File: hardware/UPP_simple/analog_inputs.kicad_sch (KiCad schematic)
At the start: 103 parts, among them J1 Conn_01x03, J10 Conn_01x04, J11 Conn_01x04, J19 Conn_01x04, J2 Conn_01x03, J3 Conn_01x03, J4 Conn_01x03, J5 Conn_01x03, J6 Conn_01x03, J7 Conn_01x04, J8 Conn_01x04, J9 Conn_01x04, U1 Opamp_Quad, U2 Opamp_Quad, U3 Opamp_Quad, U4 Opamp_Quad, U5 Opamp_Quad, U8 Opamp_Quad, U9 Opamp_Quad

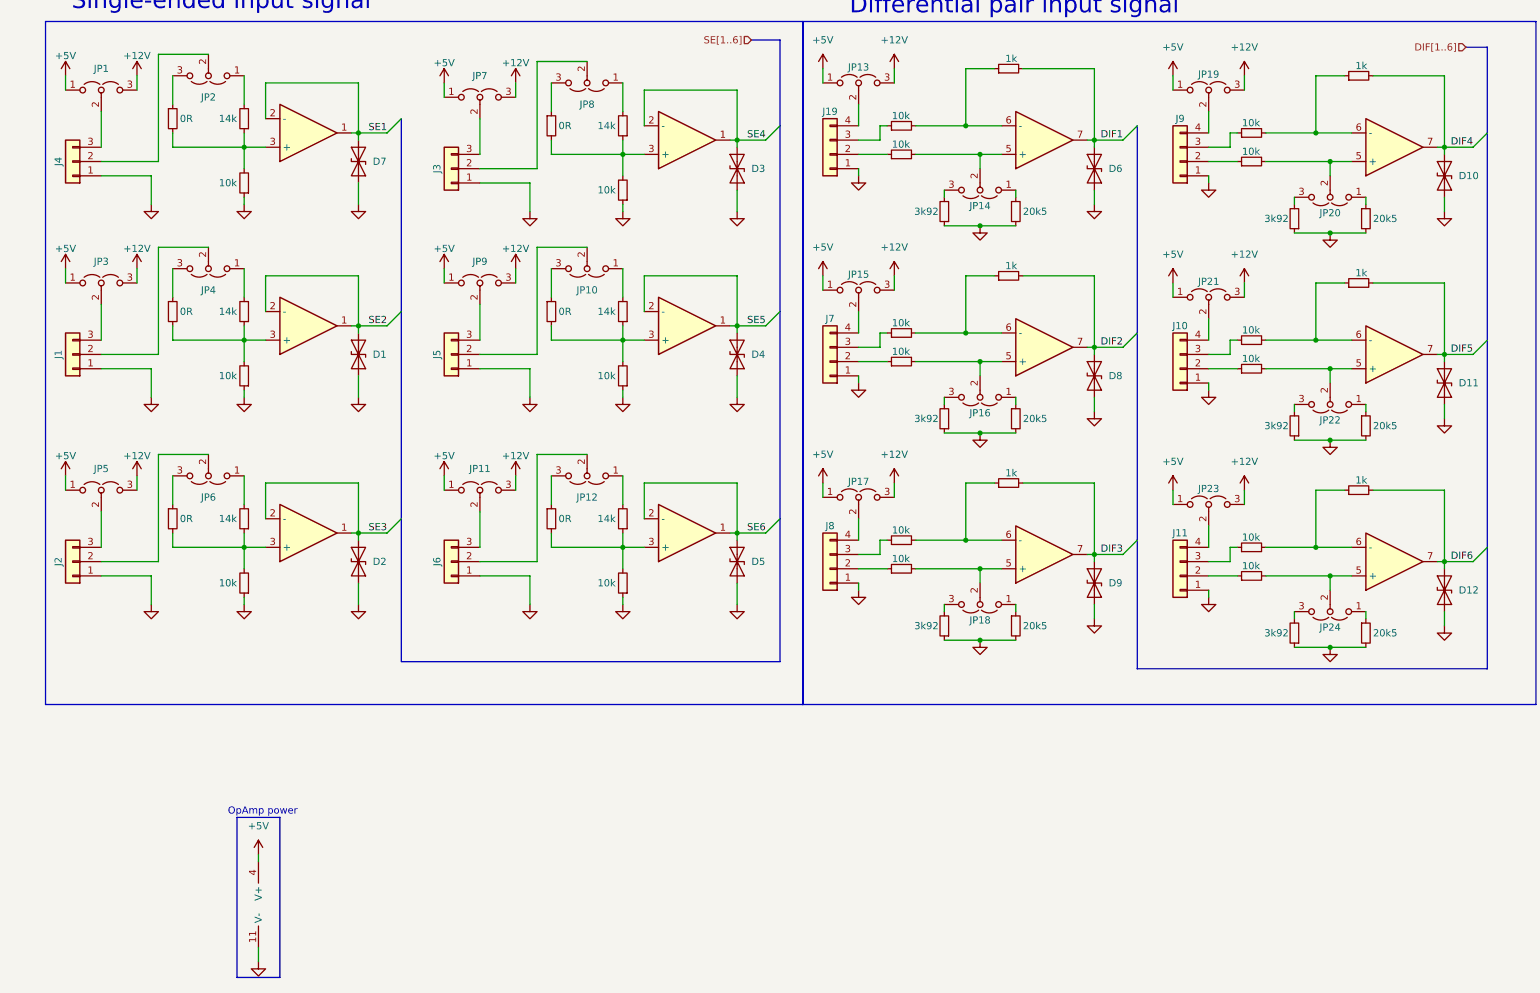
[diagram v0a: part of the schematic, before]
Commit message: Solved ERC errors and cleaned up schematic
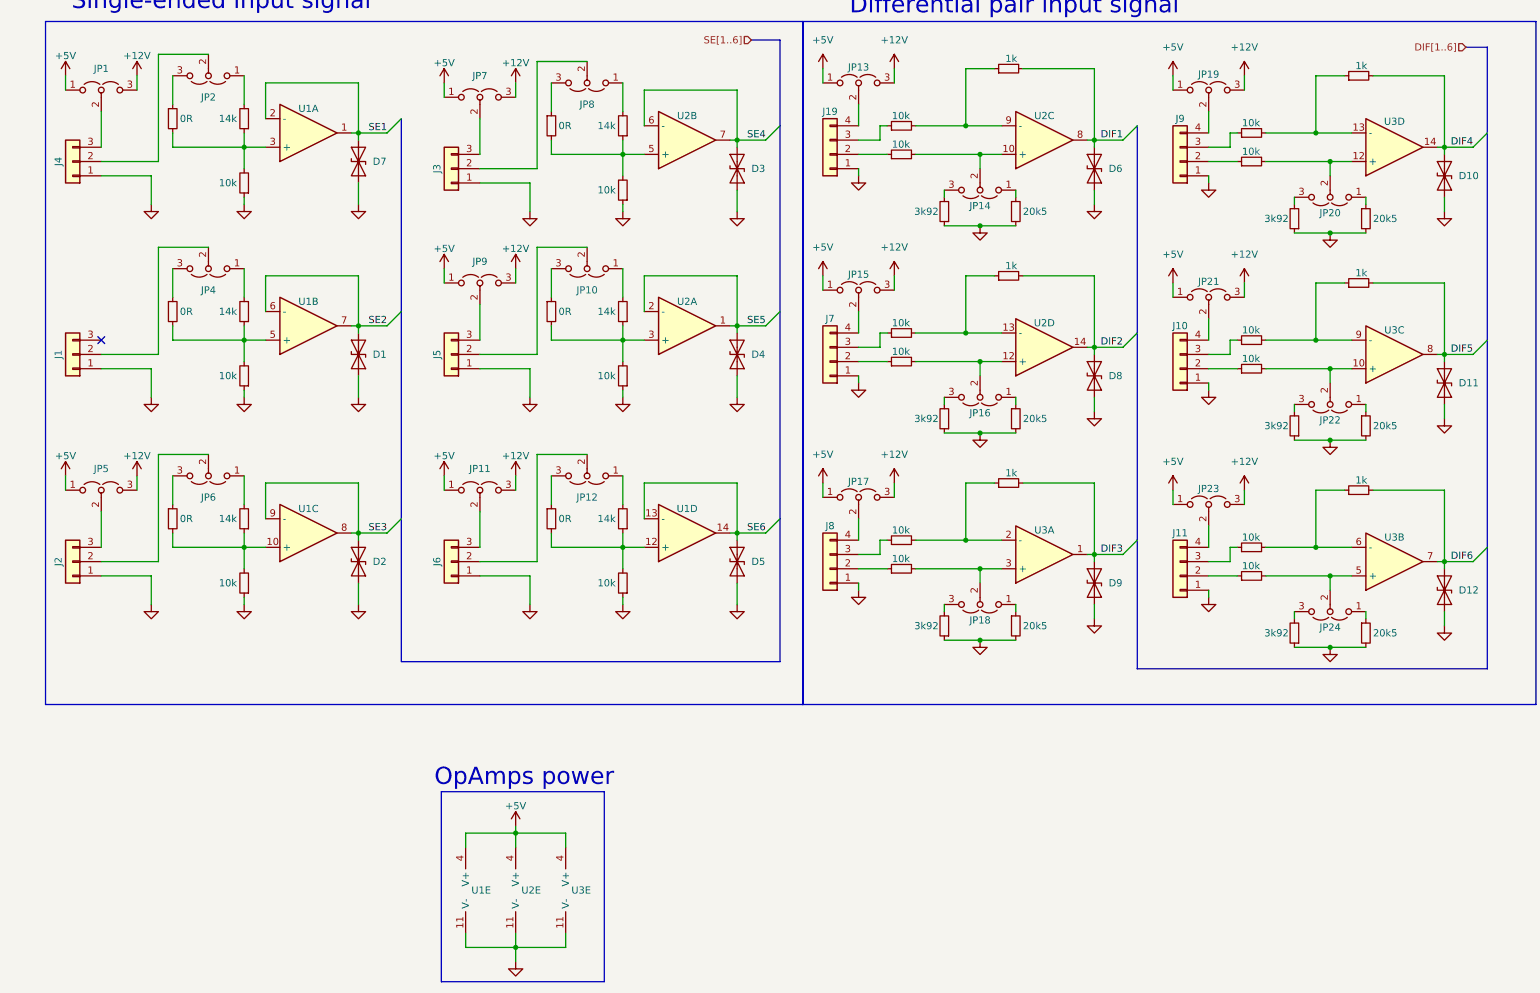
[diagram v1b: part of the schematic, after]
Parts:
- removed JP3: Jumper_3_Open, symbol Jumper:Jumper_3_Open
- removed U4, U5, U8, U9: Opamp_Quad, symbol Device:Opamp_Quad
- added unit 5 of U1
- added unit 4 of U1
- added unit 3 of U1
- added unit 3 of U2
- added unit 5 of U2
- added unit 4 of U2
- added unit 3 of U3
- added unit 5 of U3
- added unit 4 of U3
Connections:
- net +5V: now also U1.4 (V+), U2.4 (V+), U3.4 (V+)
- net DIF1: now also U2.8
- net DIF2: now also U2.14; no longer U1.7
- net DIF3: now also U3.1; no longer U2.7
- net DIF4: now also U3.14; no longer U3.7
- net DIF5: now also U3.8
- net DIF6: now also U3.7
- net GND: now also U1.11 (V-), U2.11 (V-), U3.11 (V-)
- net SE1: now also U1.1, U1.2 (-)
- net SE2: now also U1.6 (-), U1.7; no longer U1.1, U1.2 (-)
- net SE3: now also U1.8, U1.9 (-); no longer U2.1, U2.2 (-)
- net SE4: now also U2.6 (-), U2.7; no longer U3.1, U3.2 (-)
- net SE5: now also U2.1, U2.2 (-)
- net SE6: now also U1.13 (-), U1.14
- net at R1.2, R2.1, R3.2: now also U1.5 (+); no longer U1.3 (+)
- net at R17.1, R18.2, R33.2: now also U1.3 (+)
- net at R43.2, R52.1: now also U3.9 (-)
- net at R36.2, R39.1: now also U3.2 (-); no longer U2.6 (-)
- net at JP22.2 (C), R44.2: now also U3.10 (+)
- net at R20.2, R21.1, R22.2: now also U2.3 (+)
- net at R32.1, R8.2: now also U2.9 (-)
- net at JP14.2 (C), R28.2: now also U2.10 (+)
- net at R41.2, R50.1: now also U3.13 (-); no longer U3.6 (-)
- net at JP20.2 (C), R42.2: now also U3.12 (+); no longer U3.5 (+)
- net at R16.1, R19.2, R7.2: now also U2.5 (+); no longer U3.3 (+)
- net at R45.2, R54.1: now also U3.6 (-)
- net at JP16.2 (C), R27.2: now also U2.12 (+); no longer U1.5 (+)
- net at R26.2, R34.1: now also U2.13 (-); no longer U1.6 (-)
- net at JP18.2 (C), R37.2: now also U3.3 (+); no longer U2.5 (+)
- net at R4.2, R5.1, R6.2: now also U1.10 (+); no longer U2.3 (+)
- net at JP24.2 (C), R46.2: now also U3.5 (+)
- net at R23.2, R24.1, R25.2: now also U1.12 (+)
- no-connect marks 0 -> 1
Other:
- note added: "OpAmps power"
- note removed: "OpAmp power"

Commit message: Add files via upload
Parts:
- removed J19, J7, J8: Conn_01x04, symbol Connector_Generic:Conn_01x04
- removed JP1, JP10, JP11, JP12, JP13, JP14, JP15, JP16, JP17, JP18, JP19, JP2, JP20, JP21, JP22, JP23, JP24, JP4, JP5, JP6, JP7, JP8, JP9: Jumper_3_Open, symbol Jumper:Jumper_3_Open
- removed U2, U3: Opamp_Quad, symbol Device:Opamp_Quad
- added C21, C22, C23: 100n, Capacitor_SMD:C_0603_1608Metric, symbol Device:C_Small
- added J12, J13, J14: Conn_01x04, symbol Connector_Generic:Conn_01x04
- added JP1, JP10, JP11, JP13, JP14, JP15, JP16, JP17, JP18, JP19, JP2, JP20, JP21, JP22, JP23, JP24, JP25, JP26, JP3, JP31, JP32, JP33, JP34, JP35, JP36, JP37, JP38, JP39, JP4, JP40, JP41, JP42, JP43, JP44, JP45, JP46, JP47, JP5, JP6, JP7, JP8, JP9: SolderJumper_3_Bridged12, Jumper:SolderJumper-3_P1.3mm_Bridged12_Pad1.0x1.5mm, symbol Jumper:SolderJumper_3_Bridged12
- added R64, R66, R67, R68, R69, R71, R72, R74, R75, R76, R77, R79, R80: 10k, Resistor_SMD:R_0603_1608Metric_Pad0.98x0.95mm_HandSolder, symbol Device:R_Small
- added R65, R73, R81: 5k, Resistor_SMD:R_0603_1608Metric_Pad0.98x0.95mm_HandSolder, symbol Device:R_Small
- added R70, R78: 12k, Resistor_SMD:R_0603_1608Metric_Pad0.98x0.95mm_HandSolder, symbol Device:R_Small
- added U8, U9: Opamp_Quad, Footprints:SOP65P640X120-14N, symbol Device:Opamp_Quad
- R29, R38: value 3k92 -> 12k
- R30, R35, R40, R51, R53, R55: value 20k5 -> 10k
- R31, R47, R48: value 3k92 -> 10k
- R32: value 1k -> 5k
- R34, R39, R50, R52: value 1k -> 10k
- R41: value 10k -> 5k
- R46: value 10k -> 12k
- R49: value 3k92 -> 5k
- R54: value 1k -> 12k
- U7: renamed from U1; footprint (none) -> Footprints:SOP65P640X120-14N
- renumbered J4 to J3, J1 to J4, J2 to J5, J3 to J6, J5 to J7, J6 to J8
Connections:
- net +12V: now also JP1.3 (B), JP10.3 (B), JP11.3 (B), JP13.3 (B), JP18.3 (B), JP2.3 (B), JP23.3 (B), JP26.3 (B), JP33.3 (B), JP38.3 (B), JP43.3 (B), JP9.3 (B)
- net +5V: now also C21.1, C22.1, C23.1, JP1.1 (A), JP10.1 (A), JP11.1 (A), JP13.1 (A), JP18.1 (A), JP2.1 (A), JP23.1 (A), JP26.1 (A), JP33.1 (A), JP38.1 (A), JP43.1 (A), JP9.1 (A), U8.4 (V+), U9.4 (V+)
- net DIF1: now also R31.2, U8.8
- net DIF2: now also R40.2, R41.2, U8.14; no longer R34.2
- net DIF3: now also R48.2, R49.2, U9.1; no longer R39.2
- net DIF4: now also R64.2, R65.2, U9.14; no longer R50.2
- net DIF5: now also R72.2, R73.2, U9.8; no longer R52.2
- net DIF6: now also R80.2, R81.2, U9.7; no longer R54.2
- net GND: now also R29.2, R38.2, R39.2, R46.2, R47.2, R54.2, C21.2, C22.2, C23.2, J12.1 (Pin_1), J13.1 (Pin_1), J14.1 (Pin_1), R70.2, R71.2, R78.2, R79.2, U8.11 (V-), U9.11 (V-); no longer R29.1, R31.1, R35.2, R38.1, R40.2, R47.1, R48.1, R49.1, R51.2, R53.2
- net SE4: now also U8.6 (-), U8.7
- net SE5: now also U8.1, U8.2 (-)
- net at J9.4 (Pin_4): now also JP13.2 (C)
- net at R1.1: now also JP3.1 (A)
- net at J11.2 (Pin_2): now also JP25.2 (C); no longer R46.1
- net at R45.1: now also JP25.3 (B); no longer J11.3 (Pin_3)
- net at J11.4 (Pin_4): now also JP23.2 (C)
- net at R43.2: now also R42.2, JP31.2 (C), U9.2 (-); no longer R52.1
- net at R53.1: now also JP35.3 (B)
- net at R39.1: now also JP22.1 (A); no longer R36.2
- net at R27.1: now also JP15.1 (A)
- net at R26.1: now also JP14.3 (B)
- net at R32.1: now also JP16.3 (B); no longer R8.2
- net at R28.1: now also JP15.3 (B)
- net at R28.2: now also R27.2, JP17.2 (C), U8.10 (+)
- net at J3.3 (Pin_3): now also JP2.2 (C)
- net at R50.1: now also JP34.1 (A); no longer R41.2
- net at R17.2: now also JP4.3 (B)
- net at J3.2 (Pin_2): now also JP4.2 (C)
- net at R33.1: now also JP4.1 (A)
- net at R21.2: now also JP7.3 (B)
- net at J7.2 (Pin_2): now also JP7.2 (C)
- net at R20.1: now also JP7.1 (A)
- net at J6.3 (Pin_3): now also JP9.2 (C)
- net at R16.1, R19.2, R7.2: now also U8.5 (+)
- net at R16.2: now also JP8.3 (B)
- net at R30.1: now also JP17.1 (A)
- net at J7.3 (Pin_3): now also JP10.2 (C)
- net at R45.2: now also R44.2, JP32.2 (C), U9.3 (+); no longer R54.1
- net at R7.1: now also JP8.1 (A)
- net at J4.2 (Pin_2): now also JP3.2 (C)
- net at J4.3 (Pin_3): now also JP1.2 (C)
- net at R36.1: now also JP20.1 (A)
- net at R37.1: now also JP20.3 (B)
- net at R37.2: now also R36.2, JP22.2 (C), U8.12 (+)
- net at R20.2, R21.1, R22.2: now also U8.3 (+)
- net at R55.1: now also JP37.1 (A)
- net at R2.2: now also JP3.3 (B)
- net at R44.1: now also JP25.1 (A); no longer J10.2 (Pin_2)
- net at J10.3 (Pin_3): now also JP19.2 (C); no longer R43.1
- net at J10.4 (Pin_4): now also JP18.2 (C)
- net at R35.1: now also JP19.3 (B)
- net at R34.1: now also JP19.1 (A); no longer R26.2
- net at J8.3 (Pin_3): now also JP11.2 (C)
- net at J8.2 (Pin_2): now also JP6.2 (C)
- net at R4.1: now also JP5.1 (A)
- net at R8.1: now also JP14.1 (A)
- net at R40.1: now also JP21.1 (A)
- net at J9.2 (Pin_2): now also JP15.2 (C); no longer R42.1
- net at J9.3 (Pin_3): now also JP14.2 (C); no longer R41.1
- net at R23.1: now also JP6.1 (A)
- net at J5.3 (Pin_3): now also JP26.2 (C)
- net at R51.1: now also JP34.3 (B)
- net at R5.2: now also JP5.3 (B)
- net at R24.2: now also JP6.3 (B)
- net at J6.2 (Pin_2): now also JP8.2 (C)
- net at J5.2 (Pin_2): now also JP5.2 (C)
- new net: JP31.1 (A), R48.1
- new net: JP31.3 (B), R49.1
- new net: JP32.1 (A), R47.1
- new net: JP41.1 (A), R72.1
- new net: JP37.3 (B), R54.1
- new net: JP36.1 (A), R64.1
- new net: JP40.1 (A), R68.1
- new net: J13.2 (Pin_2), JP40.2 (C)
- new net: JP40.3 (B), R69.1
- new net: JP41.2 (C), R66.2, R67.2, U9.9 (-)
- new net: JP41.3 (B), R73.1
- new net: JP47.1 (A), R79.1
- new net: JP47.2 (C), R76.2, R77.2, U9.5 (+)
- new net: JP47.3 (B), R78.1
- new net: JP22.3 (B), R38.1
- new net: J10.2 (Pin_2), JP20.2 (C)
- new net: JP46.3 (B), R81.1
- new net: JP36.3 (B), R65.1
- new net: JP45.1 (A), R76.1
- new net: J14.2 (Pin_2), JP45.2 (C)
- new net: JP45.3 (B), R77.1
- new net: JP36.2 (C), R50.2, R51.2, U9.13 (-)
- new net: JP21.2 (C), R34.2, R35.2, U8.13 (-)
- new net: JP16.1 (A), R31.1
- new net: JP44.1 (A), R74.1
- new net: J14.3 (Pin_3), JP44.2 (C)
- new net: JP44.3 (B), R75.1
- new net: JP37.2 (C), R52.2, R53.2, U9.12 (+)
- new net: J13.3 (Pin_3), JP39.2 (C)
- new net: J13.4 (Pin_4), JP38.2 (C)
- new net: JP16.2 (C), R26.2, R8.2, U8.9 (-)
- new net: JP46.2 (C), R74.2, R75.2, U9.6 (-)
- new net: J11.3 (Pin_3), JP24.2 (C)
- new net: JP35.1 (A), R52.1
- new net: JP42.1 (A), R71.1
- new net: JP42.2 (C), R68.2, R69.2, U9.10 (+)
- new net: JP42.3 (B), R70.1
- new net: JP39.1 (A), R66.1
- new net: JP39.3 (B), R67.1
- new net: JP17.3 (B), R29.1
- new net: J12.2 (Pin_2), JP35.2 (C)
- new net: J12.3 (Pin_3), JP34.2 (C)
- new net: J12.4 (Pin_4), JP33.2 (C)
- new net: JP32.3 (B), R46.1
- new net: JP21.3 (B), R41.1
- new net: JP46.1 (A), R80.1
- new net: JP24.1 (A), R42.1
- new net: JP24.3 (B), R43.1
- new net: J14.4 (Pin_4), JP43.2 (C)
- no-connect marks 1 -> 0
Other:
- moved on the sheet: U7E
